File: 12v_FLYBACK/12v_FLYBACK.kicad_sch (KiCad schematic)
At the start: 27 parts, among them J1 AC Input, T1 Transformer_1P_2S

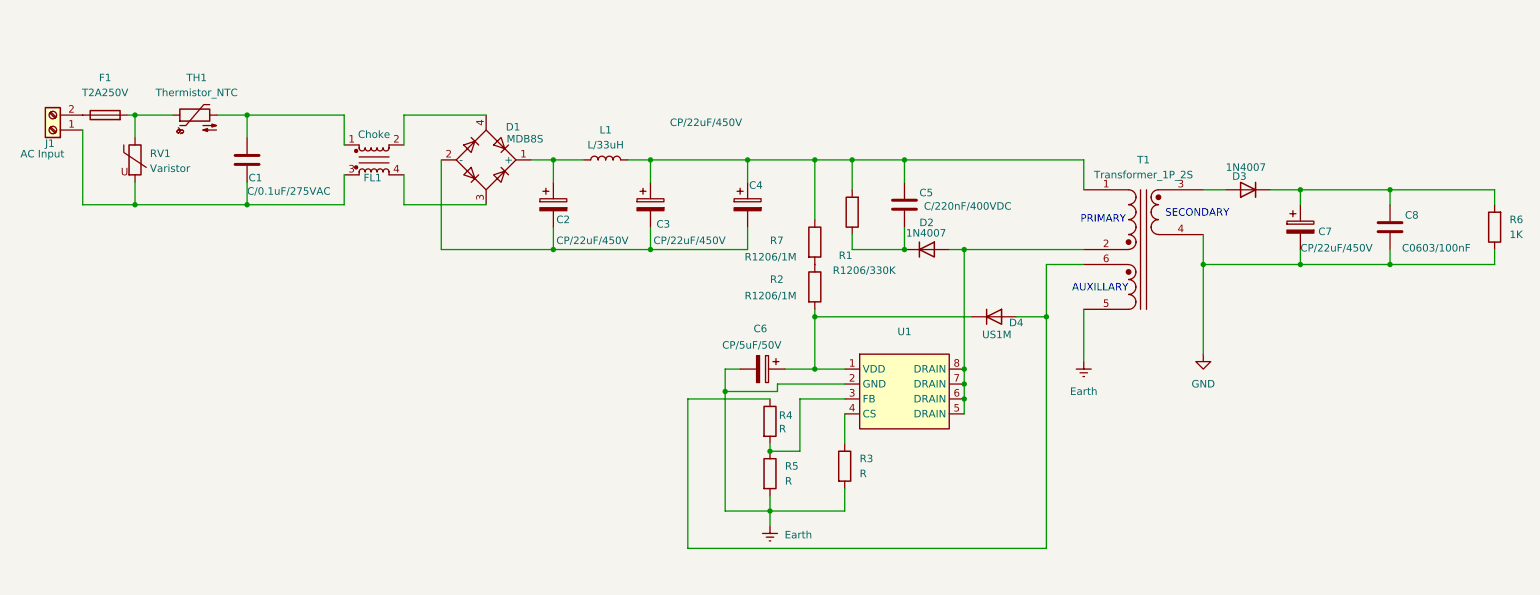
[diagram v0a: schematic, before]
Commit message: Change controller IC
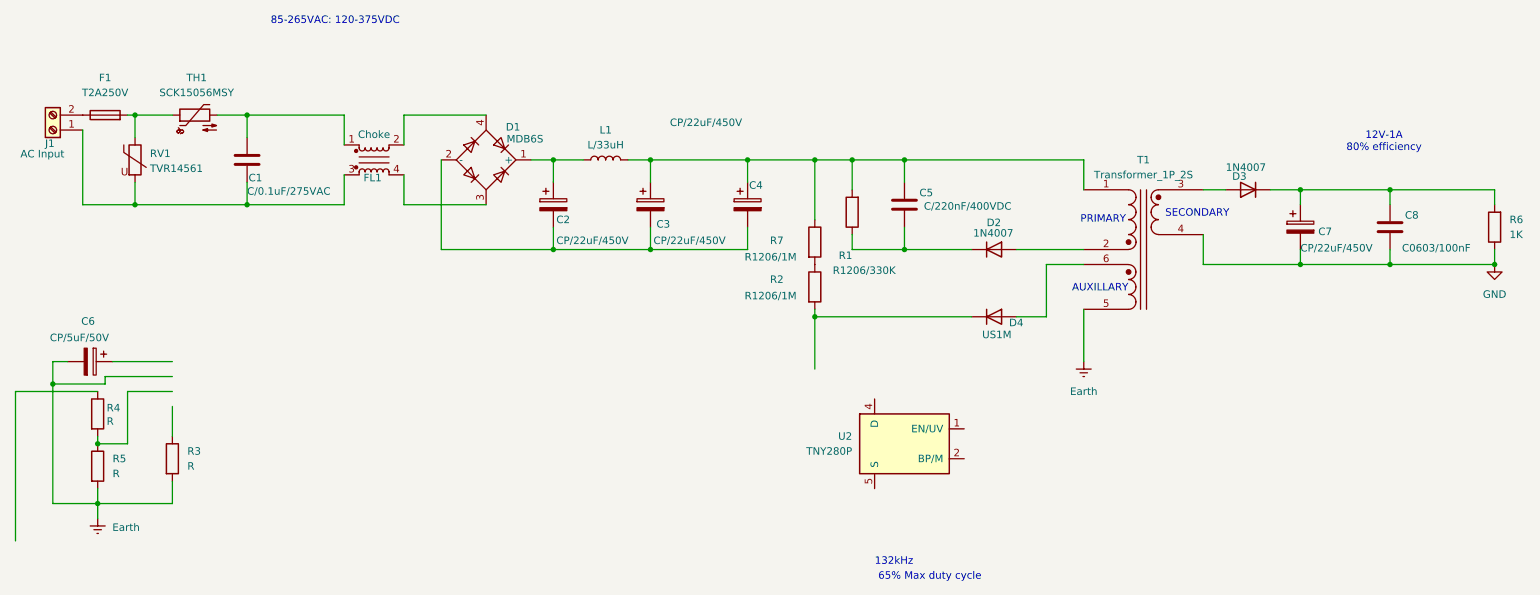
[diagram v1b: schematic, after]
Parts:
- removed U1: ~, Package_DIP:DIP-8_W7.62mm, symbol HARDWARE_DFM:KP21827
- added U2: TNY280P, Package_DIP:PowerIntegrations_PDIP-8C, symbol Regulator_Switching:TNY280P
- D1: value MDB8S -> MDB6S
- F1: footprint MinhDfm:FUSE_T2A250V -> Fuse:Fuse_Littelfuse_395Series
- RV1: value Varistor -> TVR14561; footprint (none) -> Varistor:RV_Disc_D15.5mm_W3.9mm_P7.5mm
- TH1: value Thermistor_NTC -> SCK15056MSY
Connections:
- net at D4.1 (K), R2.2: no longer C6.1
- net at D4.2 (A), T1.6 (SD): no longer R4.1
- new net: U2.5 (S), U2.6 (S), U2.7 (S), U2.8 (S)
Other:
- note added: "12V-1A 80% efficiency"
- note added: "132kHz"
- note added: "65% Max duty cycle"
- note added: "85-265VAC: 120-375VDC"
- moved on the sheet: C6, D2, R3, R4, R5
